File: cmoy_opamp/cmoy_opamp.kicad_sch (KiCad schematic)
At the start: 51 parts, among them J1 AudioJack3, J2 AudioJack3, SW1 SPST, U1 OPA2227, U2 LMH6642, U3 OPA134, U4 OPA134

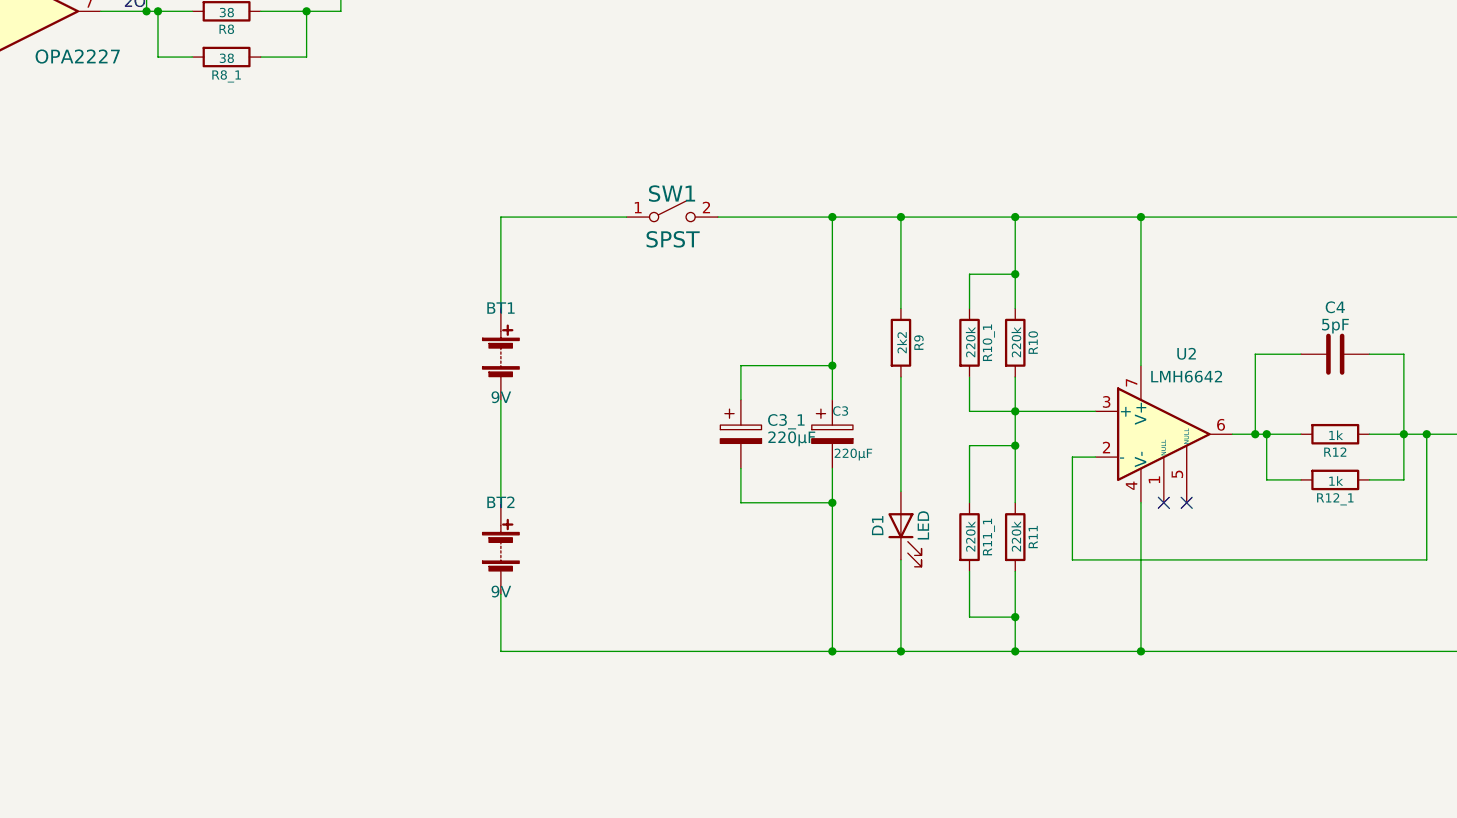
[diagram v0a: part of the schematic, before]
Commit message: Add TLE2426 as option
TLE2426 option alternative to R10/R11 voltage divider
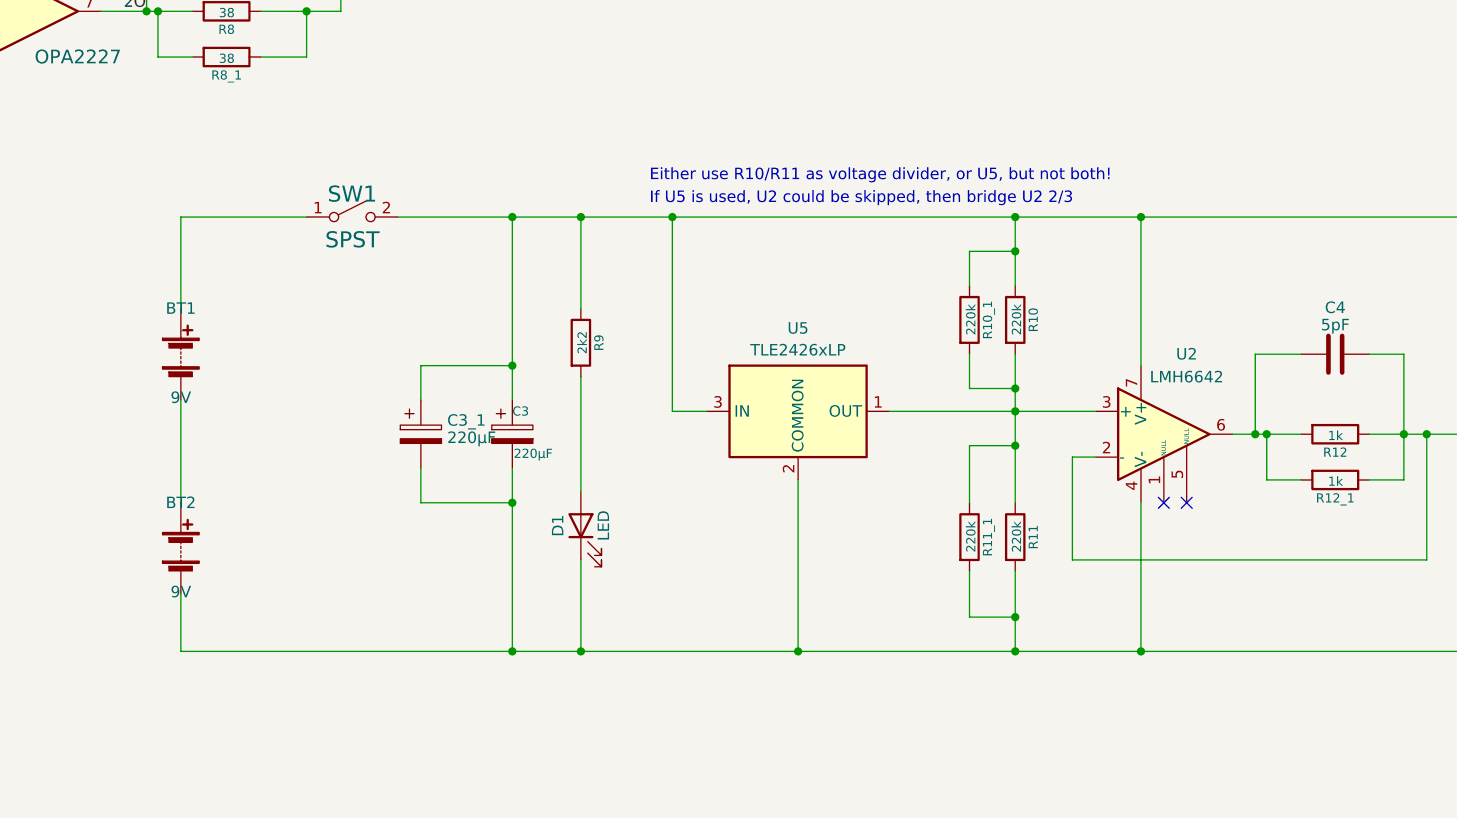
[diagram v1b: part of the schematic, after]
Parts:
- added U5: TLE2426xLP, Package_TO_SOT_THT:TO-92, symbol Reference_Voltage:TLE2426xLP
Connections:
- net V+: now also U5.3 (IN)
- net V-: now also U5.2 (COMMON)
- net at R10.2, R10_1.2, R11.1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: now also U5.1 (OUT)
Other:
- note added: "Either use R10/R11 as voltage divider, or U5, but not both!"
- note added: "If U5 is used, U2 could be skipped, then bridge U2 2/3"
- moved on the sheet: BT1, BT2, C3, C3_1, D1, R10, R10_1, R9, SW1
